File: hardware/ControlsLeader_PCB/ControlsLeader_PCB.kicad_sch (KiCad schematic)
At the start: 16 parts, among them J1 CarCANConnector_Out, J15 Conn_01x04, J16 SteeringConn_01x05, J17 Conn_01x02, J2 PeripheralCAN_out, J3 CarCANConnector_In, J4 PeripheralCAN_in, J6 DashConn1_2Rows-09Pins, J7 Dash_LSOM_PWR, J8 DashConn2_2Rows-09Pins, U2 LeaderSOM

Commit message: Schematic RevA
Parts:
- removed J6: DashConn1_2Rows-09Pins, Connector_Molex:Molex_Nano-Fit_105313-xx08_1x08_P2.50mm_Horizontal, symbol Connector_Generic:Conn_2Rows-09Pins
- removed J8: DashConn2_2Rows-09Pins, Connector_Molex:Molex_Nano-Fit_105313-xx08_1x08_P2.50mm_Horizontal, symbol Connector_Generic:Conn_2Rows-09Pins
- added D29: 1N4148WT, Diode_SMD:D_SOD-523, symbol Diode:1N4148WT
- added J18: Lights_PWR, UTSVT_Connectors:AMASS_XT30PW-M_1x02_P2.50mm_Horizontal, symbol utsvt_connectors:CarLVPowerConnector
- added J19: Horn_PWR, UTSVT_Connectors:AMASS_XT30PW-M_1x02_P2.50mm_Horizontal, symbol utsvt_connectors:CarLVPowerConnector
- added J6: Conn_2Rows-13Pins, Connector_Molex:Molex_Nano-Fit_105314-xx12_2x06_P2.50mm_Horizontal, symbol Connector_Generic:Conn_2Rows-13Pins
- J15: value Conn_01x04 -> IgnConn_01x04
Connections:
- net +24V: no longer J2.1 (24V), J4.1 (24V)
- net 3.3V_LDO: now also J6.1 (Pin_1), J6.3 (Pin_3), J6.5 (Pin_5), J6.7 (Pin_7), J6.9 (Pin_9)
- net Cruise_Enable_GPIO_IN: now also J6.4 (Pin_4)
- net Cruise_Set_GPIO_IN: now also J6.2 (Pin_2)
- net Fwd_SW_GPIO: now also J6.12 (Pin_12)
- net GND: now also J18.2 (GND), J19.2 (GND)
- net Hazard_GPIO_IN: now also J6.8 (Pin_8)
- net Horn_24V_Signal_Out: now also D29.2 (A)
- net Neutral_Gear_GPIO: now also J6.11 (Pin_11)
- net Regen_Enable_GPIO_IN: now also J6.6 (Pin_6)
- net Rev_SW_GPIO: now also J6.10 (Pin_10)
- net +24v_Horn: now reaches J17.2 (Pin_2)
- net +24v_Horn: now also D29.1 (K), J19.1 (+24V)
- new net +24v_Lights: J18.1 (+24V), J2.1 (24V), J4.1 (24V)
- no-connect marks 7 -> 4
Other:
- moved on the sheet: J15, J17, J7, U2A, U2B

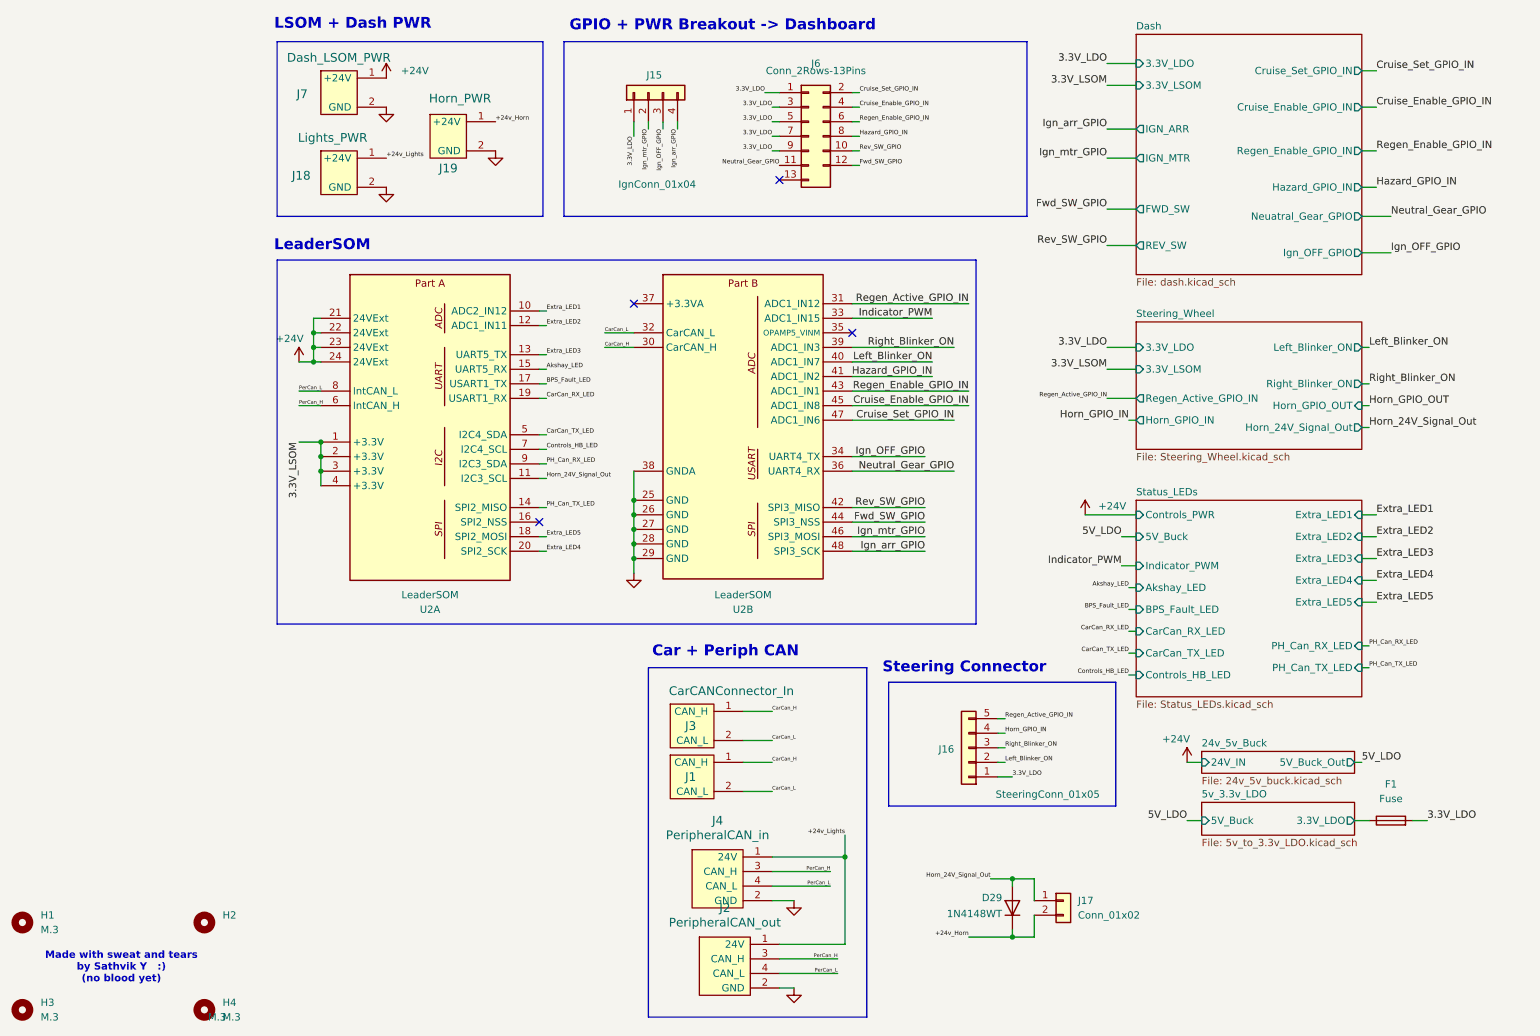
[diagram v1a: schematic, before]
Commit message: PCB DESIGN DONE - need to add datasheets and p/n
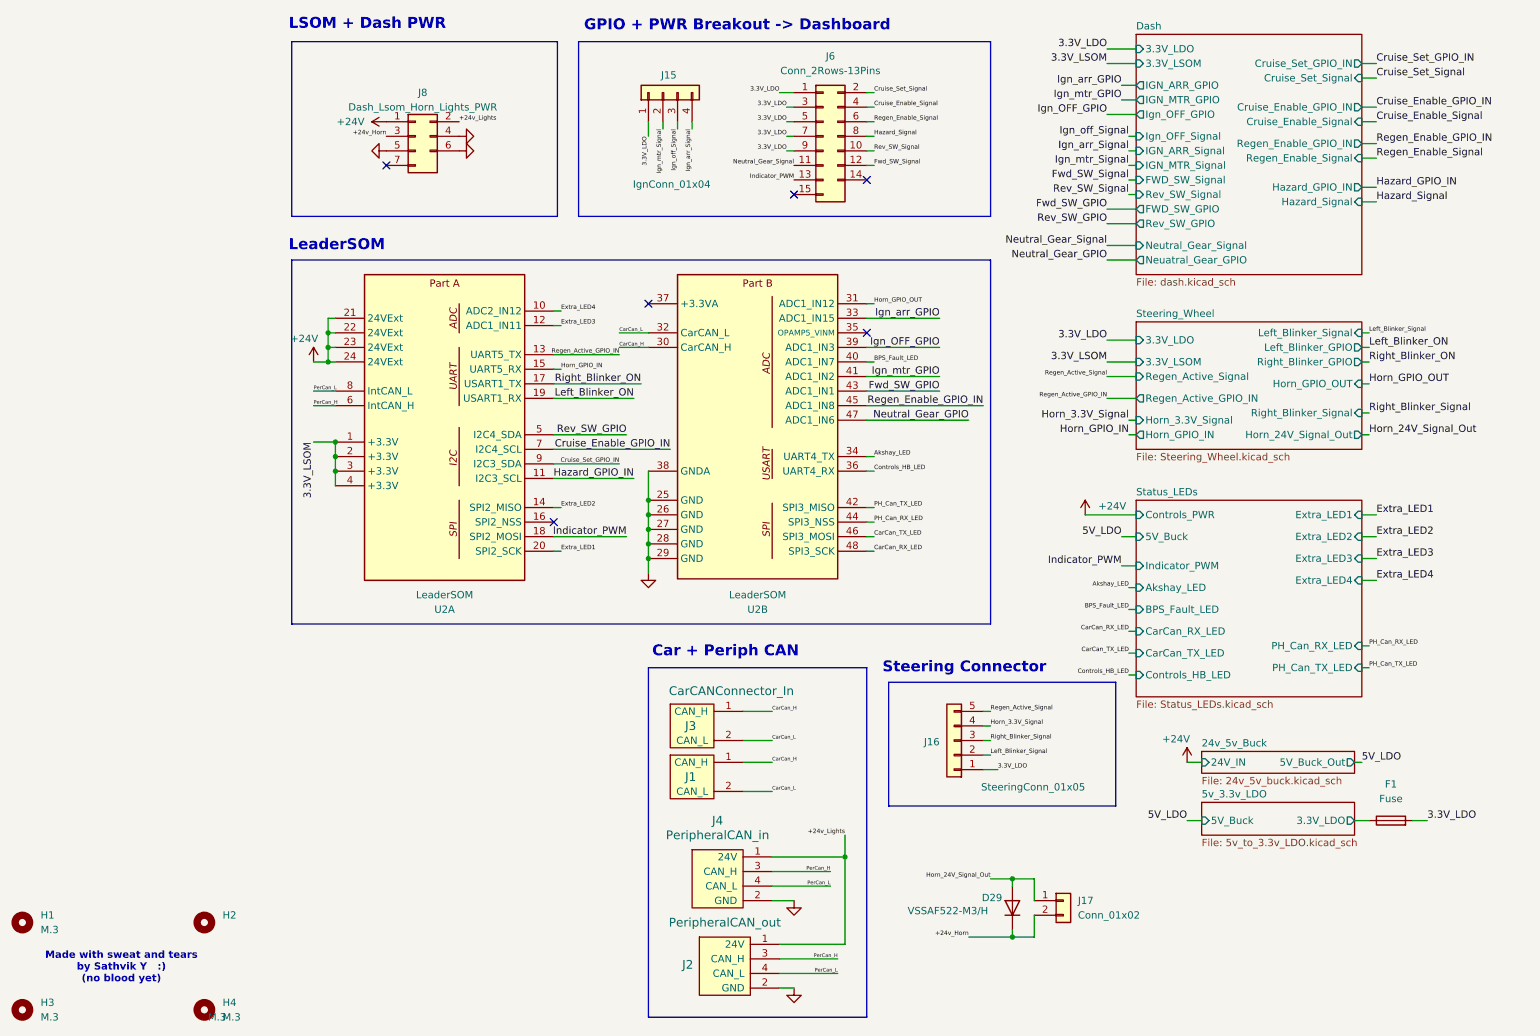
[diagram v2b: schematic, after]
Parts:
- removed J18: Lights_PWR, UTSVT_Connectors:AMASS_XT30PW-M_1x02_P2.50mm_Horizontal, symbol utsvt_connectors:CarLVPowerConnector
- removed J19: Horn_PWR, UTSVT_Connectors:AMASS_XT30PW-M_1x02_P2.50mm_Horizontal, symbol utsvt_connectors:CarLVPowerConnector
- removed J7: Dash_LSOM_PWR, UTSVT_Connectors:AMASS_XT30PW-M_1x02_P2.50mm_Horizontal, symbol utsvt_connectors:CarLVPowerConnector
- added J8: Dash_Lsom_Horn_Lights_PWR, Connector_Molex:Molex_Nano-Fit_105314-xx06_2x03_P2.50mm_Horizontal, symbol Connector_Generic:Conn_2Rows-07Pins
- D29: value 1N4148WT -> VSSAF522-M3/H
- J1, J3: footprint UTSVT_Connectors:Molex_Nano-Fit_105309-xx02_1x02_P2.50mm_Vertical -> Connector_Molex:Molex_Nano-Fit_105313-xx02_1x02_P2.50mm_Horizontal
- J2, J4: footprint UTSVT_Connectors:Molex_Nano-Fit_105309-xx04_1x04_P2.50mm_Vertical -> Connector_Molex:Molex_Nano-Fit_105313-xx04_1x04_P2.50mm_Horizontal
- J6: footprint Connector_Molex:Molex_Nano-Fit_105314-xx12_2x06_P2.50mm_Horizontal -> Connector_Molex:Molex_Nano-Fit_105314-xx14_2x07_P2.50mm_Horizontal; symbol Connector_Generic:Conn_2Rows-13Pins -> Connector_Generic:Conn_2Rows-15Pins
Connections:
- net Extra_LED5 is gone; now on net Indicator_PWM: U2.18 (SPI2_MOSI)
- net +24V: now also J8.1 (Pin_1)
- net +24v_Horn: now also J8.3 (Pin_3)
- net +24v_Lights: now also J8.2 (Pin_2)
- net Akshay_LED: now also U2.34 (UART4_TX); no longer U2.15 (UART5_RX)
- net BPS_Fault_LED: now also U2.40 (ADC1_IN7); no longer U2.17 (USART1_TX)
- net CarCan_RX_LED: now also U2.48 (SPI3_SCK); no longer U2.19 (USART1_RX)
- net CarCan_TX_LED: now also U2.46 (SPI3_MOSI); no longer U2.5 (I2C4_SDA)
- net Controls_HB_LED: now also U2.36 (UART4_RX); no longer U2.7 (I2C4_SCL)
- net Cruise_Enable_GPIO_IN: now also U2.7 (I2C4_SCL); no longer J6.4 (Pin_4), U2.45 (ADC1_IN8)
- net Cruise_Set_GPIO_IN: now also U2.9 (I2C3_SDA); no longer J6.2 (Pin_2), U2.47 (ADC1_IN6)
- net Extra_LED1: now also U2.20 (SPI2_SCK); no longer U2.10 (ADC2_IN12)
- net Extra_LED2: now also U2.14 (SPI2_MISO); no longer U2.12 (ADC1_IN11)
- net Extra_LED3: now also U2.12 (ADC1_IN11); no longer U2.13 (UART5_TX)
- net Extra_LED4: now also U2.10 (ADC2_IN12); no longer U2.20 (SPI2_SCK)
- net Fwd_SW_GPIO: now also U2.43 (ADC1_IN1); no longer J6.12 (Pin_12), U2.44 (SPI3_NSS)
- net GND: now also J8.4 (Pin_4), J8.5 (Pin_5), J8.6 (Pin_6)
- net Hazard_GPIO_IN: now also U2.11 (I2C3_SCL); no longer J6.8 (Pin_8), U2.41 (ADC1_IN2)
- net Horn_24V_Signal_Out: no longer U2.11 (I2C3_SCL)
- net Horn_GPIO_IN: now also U2.15 (UART5_RX); no longer J16.4 (Pin_4)
- net Horn_GPIO_OUT: now also U2.31 (ADC1_IN12)
- net Ign_OFF_GPIO: now also U2.39 (ADC1_IN3); no longer J15.3 (Pin_3), U2.34 (UART4_TX)
- net Ign_arr_GPIO: now also U2.33 (ADC1_IN15); no longer J15.4 (Pin_4), U2.48 (SPI3_SCK)
- net Ign_mtr_GPIO: now also U2.41 (ADC1_IN2); no longer J15.2 (Pin_2), U2.46 (SPI3_MOSI)
- net Indicator_PWM: now also J6.13 (Pin_13); no longer U2.33 (ADC1_IN15)
- net Left_Blinker_ON: now also U2.19 (USART1_RX); no longer J16.2 (Pin_2), U2.40 (ADC1_IN7)
- net Neutral_Gear_GPIO: now also U2.47 (ADC1_IN6); no longer J6.11 (Pin_11), U2.36 (UART4_RX)
- net PH_Can_RX_LED: now also U2.44 (SPI3_NSS); no longer U2.9 (I2C3_SDA)
- net PH_Can_TX_LED: now also U2.42 (SPI3_MISO); no longer U2.14 (SPI2_MISO)
- net Regen_Active_GPIO_IN: now also U2.13 (UART5_TX); no longer J16.5 (Pin_5), U2.31 (ADC1_IN12)
- net Regen_Enable_GPIO_IN: now also U2.45 (ADC1_IN8); no longer J6.6 (Pin_6), U2.43 (ADC1_IN1)
- net Rev_SW_GPIO: now also U2.5 (I2C4_SDA); no longer J6.10 (Pin_10), U2.42 (SPI3_MISO)
- net Right_Blinker_ON: now also U2.17 (USART1_TX); no longer J16.3 (Pin_3), U2.39 (ADC1_IN3)
- new net Cruise_Enable_Signal: J6.4 (Pin_4)
- new net Cruise_Set_Signal: J6.2 (Pin_2)
- new net Fwd_SW_Signal: J6.12 (Pin_12)
- new net Hazard_Signal: J6.8 (Pin_8)
- new net Horn_3.3V_Signal: J16.4 (Pin_4)
- new net Ign_arr_Signal: J15.4 (Pin_4)
- new net Ign_mtr_Signal: J15.2 (Pin_2)
- new net Ign_off_Signal: J15.3 (Pin_3)
- new net Left_Blinker_Signal: J16.2 (Pin_2)
- new net Neutral_Gear_Signal: J6.11 (Pin_11)
- new net Regen_Active_Signal: J16.5 (Pin_5)
- new net Regen_Enable_Signal: J6.6 (Pin_6)
- new net Rev_SW_Signal: J6.10 (Pin_10)
- new net Right_Blinker_Signal: J16.3 (Pin_3)
- no-connect marks 4 -> 6
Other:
- sheet Dash ports: added Cruise_Enable_Signal, Cruise_Set_Signal, FWD_SW_GPIO, FWD_SW_Signal, Hazard_Signal, IGN_ARR_GPIO, IGN_ARR_Signal, IGN_MTR_GPIO, IGN_MTR_Signal, Ign_OFF_Signal, Neutral_Gear_Signal, Regen_Enable_Signal, Rev_SW_GPIO, Rev_SW_Signal; removed FWD_SW, IGN_ARR, IGN_MTR, REV_SW
- sheet Status_LEDs ports: added none; removed Extra_LED5
- sheet Steering_Wheel ports: added Horn_3.3V_Signal, Left_Blinker_GPIO, Left_Blinker_Signal, Regen_Active_Signal, Right_Blinker_GPIO, Right_Blinker_Signal; removed Left_Blinker_ON, Right_Blinker_ON
- moved on the sheet: J15, J16, U2A, U2B
